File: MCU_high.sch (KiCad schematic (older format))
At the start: 0 parts

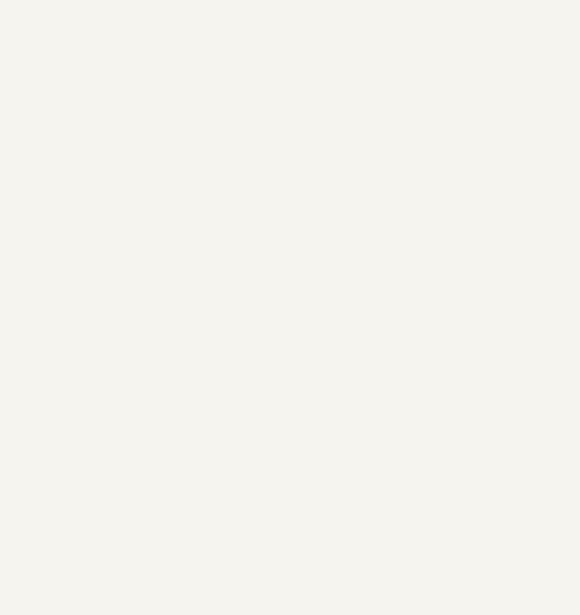
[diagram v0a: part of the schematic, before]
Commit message: - drivers modified - MCU replaced
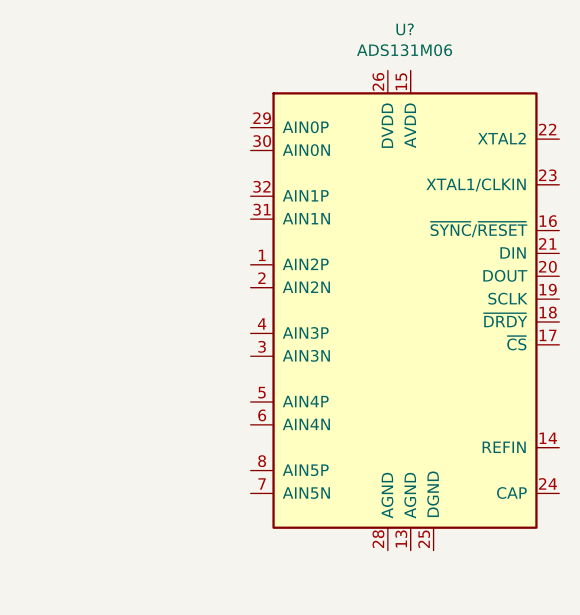
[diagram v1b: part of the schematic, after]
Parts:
- added U?: ADS131M06, miscellaneous_my:TQFP-32_5x5mm_P0.5mm_edges, symbol miscellaneous:ADS131M06
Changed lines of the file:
@@
 Text HLabel 2350 3500 0    50   Output ~ 0
 UART_TX
+$Comp
+L miscellaneous:ADS131M06 U?
+U 1 1 5F893814
+P 7850 2300
+F 0 "U?" H 7825 3528 50  0000 C CNN
+F 1 "ADS131M06" H 7825 3437 50  0000 C CNN
+F 2 "miscellaneous_my:TQFP-32_5x5mm_P0.5mm_edges" H 7850 2300 50  0001 C CNN
+F 3 "" H 7850 2300 50  0001 C CNN
+	1    7850 2300
+	1    0    0    -1
+$EndComp
 $EndSCHEMATC

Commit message: - high side (supply, MCU) - low side MCU - much small changes
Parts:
- removed U?: ADS131M06, miscellaneous_my:TQFP-32_5x5mm_P0.5mm_edges, symbol miscellaneous:ADS131M06
- added C? (x6): 100n, Capacitor_SMD:C_0603_1608Metric_Pad1.05x0.95mm_HandSolder, symbol Device:C_Small
- added C? (x6): 22p, Capacitor_SMD:C_0603_1608Metric_Pad1.05x0.95mm_HandSolder, symbol Device:C_Small
- added C?: 1u, Capacitor_SMD:C_0603_1608Metric_Pad1.05x0.95mm_HandSolder, symbol Device:C_Small
- added D?: RB520S30, miscellaneous_my:D_SOD-323-523_HandSoldering, symbol Device:D_Schottky_Small
- added J?: STLinkV2, miscellaneous_my:ST-LinkV2_FakeStm8Stm32_vertical, symbol Connector_Generic:Conn_02x05_Odd_Even
- added J?: Nucleo_SWD, Connector_PinSocket_2.54mm:PinSocket_1x06_P2.54mm_Vertical, symbol Connector:Conn_01x06_Female
- added L? (x2): BLM18TG102, Resistor_SMD:R_0603_1608Metric_Pad1.05x0.95mm_HandSolder, symbol Device:L_Core_Ferrite_Small
- added R?: 100k, Resistor_SMD:R_0603_1608Metric_Pad1.05x0.95mm_HandSolder, symbol Device:R_Small
- added R?: 0R, Resistor_SMD:R_0603_1608Metric_Pad1.05x0.95mm_HandSolder, symbol Device:R_Small
- added R?: 10R, Resistor_SMD:R_0603_1608Metric_Pad1.05x0.95mm_HandSolder, symbol Device:R_Small
- added SW?: RST, Button_Switch_SMD:SW_Push_1P1T_NO_6x6mm_H9.5mm, symbol Switch:SW_MEC_5E
- added U?: STM32L431RBTx, Package_QFP:LQFP-64_10x10mm_P0.5mm, symbol MCU_ST_STM32L4:STM32L431RBTx
- added U?: ADS131M06, miscellaneous_my:TQFP-32_5x5mm_P0.5mm_edges, symbol miscellaneous:ADS131M06
- added Y?: 8.192, Crystal:Crystal_HC49-4H_Vertical, symbol Device:Crystal_Small
- added Y?: 32.768, Crystal:Crystal_AT310_D3.0mm_L10.0mm_Horizontal_1EP_style2, symbol Device:Crystal_Small
- added Y?: 8.192, Crystal:Crystal_AT310_D3.0mm_L10.0mm_Horizontal_1EP_style2, symbol Device:Crystal_Small
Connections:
- new net: C?.2, U?.3 (PC14), Y?.1
- new net: C?.2, U?.4 (PC15), Y?.2
- new net: C?.1, U?.5 (PH0), Y?.1
- new net: C?.1, U?.6 (PH1), Y?.2
- new net: C?.1, U?.14 (REFIN)
- new net: C?.1, C?.1, L?.2, U?.15 (AVDD)
- new net: C?.1, U?.22 (XTAL2), Y?.2
- new net: C?.1, R?.1, U?.23 (XTAL1/CLKIN), Y?.1
- new net: C?.1, U?.24 (CAP)
- new net: C?.1, L?.1, L?.2
- new net: D?.2 (A), J?.1 (Pin_1), J?.8 (Pin_8)
- new net: D?.1 (K), R?.2
- new net ADC_CS: U?.17 (~CS), U?.21 (PA5)
- new net ADC_DRDY: U?.18 (~DRDY), U?.24 (PC4)
- new net ADC_MISO: U?.20 (DOUT), U?.22 (PA6)
- new net ADC_MOSI: U?.21 (DIN), U?.23 (PA7)
- new net ADC_RESET: U?.16 (~SYNC~/~RESET), U?.20 (PA4)
- new net ADC_SCK: U?.15 (PA1), U?.19 (SCLK)
- new net GND: J?.3 (Pin_3)
- new net HV+3V3: C?.1, L?.1, R?.1, R?.1, U?.26 (DVDD)
- new net HVGND: C?.1, C?.1, C?.1, C?.2, C?.2, C?.2, C?.2, C?.2, C?.2, C?.2, C?.2, C?.2, C?.2, J?.5 (Pin_5), J?.6 (Pin_6), SW?.1, SW?.2, U?.12 (VSSA), U?.13 (AGND), U?.18 (VSS), U?.25 (DGND), U?.28 (AGND), U?.31 (VSS), U?.47 (VSS), U?.63 (VSS)
- new net MCO: R?.2, U?.41 (PA8)
- new net NRST: C?.2, J?.5 (Pin_5), J?.9 (Pin_9), R?.2, SW?.3 (K), SW?.4 (A), U?.7 (NRST)
- new net SWD_CLK: J?.2 (Pin_2), J?.2 (Pin_2), U?.49 (PA14)
- new net SWD_IO: J?.4 (Pin_4), J?.4 (Pin_4), U?.46 (PA13)
- new net SWD_SWO: J?.6 (Pin_6), J?.7 (Pin_7), U?.55 (PB3)
- no-connect marks 0 -> 3

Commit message: - final schematic
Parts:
- added C159, C165, C166, C167, C168, C170: 1n, Capacitor_SMD:C_0603_1608Metric_Pad1.05x0.95mm_HandSolder, symbol Device:C_Small
- added C160, C161, C162, C163, C164: 100n, Capacitor_SMD:C_0603_1608Metric_Pad1.05x0.95mm_HandSolder, symbol Device:C_Small
- added D31: Green, Diode_SMD:D_0805_2012Metric_Pad1.15x1.40mm_HandSolder, symbol Device:LED_Small
- added D32: Orange, Diode_SMD:D_0805_2012Metric_Pad1.15x1.40mm_HandSolder, symbol Device:LED_Small
- added D33: Red, Diode_SMD:D_0805_2012Metric_Pad1.15x1.40mm_HandSolder, symbol Device:LED_Small
- added D34: Blue, Diode_SMD:D_0805_2012Metric_Pad1.15x1.40mm_HandSolder, symbol Device:LED_Small
- added R174, R176, R177, R178, R179, R181, R182: 0R, Resistor_SMD:R_0603_1608Metric_Pad1.05x0.95mm_HandSolder, symbol Device:R_Small
- added R183, R184, R185, R186: 1k, Resistor_SMD:R_0603_1608Metric_Pad1.05x0.95mm_HandSolder, symbol Device:R_Small
- added TP20, TP21, TP22, TP23: TestPoint, TestPoint:TestPoint_THTPad_D1.5mm_Drill0.7mm, symbol Connector:TestPoint
- gave numbers to parts that had none: 27
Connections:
- net HV+3V3: now also U34.13 (VDDA), U34.19 (VDD), U34.32 (VDD), U34.48 (VDDUSB), U34.64 (VDD), C160.2, C161.2, C162.2, C163.2, C164.2, R179.2
- net HVGND: now also U33.2 (AIN2N), U33.3 (AIN3N), U33.30 (AIN0N), U33.31 (AIN1N), U33.6 (AIN4N), U33.7 (AIN5N), C159.1, C160.1, C161.1, C162.1, C163.1, C164.1, C165.1, C166.1, C167.1, C168.1, C170.1, R183.2, R184.2, R185.2, R186.2
- net UART_RX: now also U34.59 (PB7)
- net UART_TX: now also U34.58 (PB6)
- net at U34.1 (VBAT): now also R179.1
- net LED_BLU: now reaches U34.50 (PA15)
- net LED_BLU: now also D34.2 (A)
- net LED_GRN: now reaches U34.51 (PC10)
- net LED_GRN: now also D31.2 (A)
- net LED_ORG: now reaches U34.52 (PC11)
- net LED_ORG: now also D32.2 (A)
- net LED_RED: now reaches U34.53 (PC12)
- net LED_RED: now also D33.2 (A)
- net at U33.1 (AIN2P): now also C166.2, R177.2
- net at U33.29 (AIN0P): now also C159.2, R174.2
- net at U33.32 (AIN1P): now also C165.2, R176.2
- net at U33.4 (AIN3P): now also C167.2, R178.2
- net at U33.5 (AIN4P): now also C168.2, R181.2
- net at U33.8 (AIN5P): now also C170.2, R182.2
- new net: D31.1 (K), R183.1
- new net: D32.1 (K), R184.1
- new net: D33.1 (K), R185.1
- new net: D34.1 (K), R186.1
- new net: R182.1, TP23.1
- new net: R181.1, TP22.1
- new net: R178.1, TP21.1
- new net: R177.1, TP20.1
- new net ADC_CH0: R174.1
- new net ADC_CH1: R176.1
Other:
- moved on the sheet: D30, J11, J12, R173

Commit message: - init PCB - fix last things in schematic
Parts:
- removed SW11: RST, Button_Switch_SMD:SW_Push_1P1T_NO_6x6mm_H9.5mm, symbol Switch:SW_MEC_5E
- added SW11: RST, Button_Switch_SMD:SW_Push_1P1T_NO_6x6mm_H9.5mm, symbol Switch:SW_Push
- added TP33, TP34, TP35, TP36, TP37, TP38, TP39, TP40, TP41, TP42, TP43, TP44, TP45, TP46: TestPoint, TestPoint:TestPoint_THTPad_D1.5mm_Drill0.7mm, symbol Connector:TestPoint
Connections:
- net HVGND: now also SW11.1
- net NRST: now also SW11.2
- net at U34.16 (PA2): now also TP33.1
- net at U34.17 (PA3): now also TP34.1
- net at U34.29 (PB10): now also TP41.1
- net at U34.30 (PB11): now also TP42.1
- net at U34.33 (PB12): now also TP43.1
- net at U34.34 (PB13): now also TP44.1
- net at U34.35 (PB14): now also TP45.1
- net at U34.36 (PB15): now also TP46.1
- net at U34.42 (PA9): now also TP35.1
- net at U34.43 (PA10): now also TP36.1
- net at U34.44 (PA11): now also TP37.1
- net at U34.45 (PA12): now also TP38.1
- net at U34.61 (PB8): now also TP39.1
- net at U34.62 (PB9): now also TP40.1

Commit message: - pcb placement, add 3dShapes
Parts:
- Y4: footprint Crystal:Crystal_AT310_D3.0mm_L10.0mm_Horizontal_1EP_style2 -> Crystal:Crystal_HC49-4H_Vertical
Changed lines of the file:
@@
 F 0 "Y4" H 10500 2400 50  0000 C CNN
 F 1 "8.192" H 10500 2300 50  0000 C CNN
-F 2 "Crystal:Crystal_AT310_D3.0mm_L10.0mm_Horizontal_1EP_style2" H 10500 2200 50  0001 C CNN
+F 2 "Crystal:Crystal_HC49-4H_Vertical" H 10500 2200 50  0001 C CNN
 F 3 "~" H 10500 2200 50  0001 C CNN
 	1    10500 2200

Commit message: - PCB progress
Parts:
- removed R179: 0R, Resistor_SMD:R_0603_1608Metric_Pad1.05x0.95mm_HandSolder, symbol Device:R_Small
- C153, C154, C155, C156, C157, C158, C159, C160, C161, C162, C163, C164, C165, C166, C167, C168, C169, C170, C171, C172, C173, C174, C175, C176: footprint Capacitor_SMD:C_0603_1608Metric_Pad1.05x0.95mm_HandSolder -> Capacitor_SMD:C_0603_1608Metric
- L14, L15: footprint Resistor_SMD:R_0603_1608Metric_Pad1.05x0.95mm_HandSolder -> Inductor_SMD:L_0603_1608Metric
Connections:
- net GND is gone; now on net HVGND: J12.3 (Pin_3)
- net HV+3V3: now also U34.1 (VBAT)

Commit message: - PCB WiP - Pump output aligned
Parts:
- R173, R174, R175, R176, R177, R178, R180, R181, R182, R183, R184, R185, R186: footprint Resistor_SMD:R_0603_1608Metric_Pad1.05x0.95mm_HandSolder -> Resistor_SMD:R_0603_1608Metric
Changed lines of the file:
@@
 F 0 "R180" H 3409 3396 50  0000 L CNN
 F 1 "100k" H 3409 3305 50  0000 L CNN
-F 2 "Resistor_SMD:R_0603_1608Metric_Pad1.05x0.95mm_HandSolder" H 3350 3350 50  0001 C CNN
+F 2 "Resistor_SMD:R_0603_1608Metric" H 3350 3350 50  0001 C CNN
 F 3 "~" H 3350 3350 50  0001 C CNN
 	1    3350 3350
@@
 F 0 "R175" V 10900 2500 50  0000 C BNN
 F 1 "0R" V 10700 2500 50  0000 C TNN
-F 2 "Resistor_SMD:R_0603_1608Metric_Pad1.05x0.95mm_HandSolder" V 10730 2500 50  0001 C CNN
+F 2 "Resistor_SMD:R_0603_1608Metric" V 10730 2500 50  0001 C CNN
 F 3 "~" H 10800 2500 50  0001 C CNN
 	1    10800 2500
@@
 F 0 "R173" H 2109 1146 50  0000 L CNN
 F 1 "10R" H 2109 1055 50  0000 L CNN
-F 2 "Resistor_SMD:R_0603_1608Metric_Pad1.05x0.95mm_HandSolder" H 2050 1100 50  0001 C CNN
+F 2 "Resistor_SMD:R_0603_1608Metric" H 2050 1100 50  0001 C CNN
 F 3 "~" H 2050 1100 50  0001 C CNN
 	1    2050 1100
@@
 F 0 "R183" H 959 3946 50  0000 L CNN
 F 1 "1k" H 959 3855 50  0000 L CNN
-F 2 "Resistor_SMD:R_0603_1608Metric_Pad1.05x0.95mm_HandSolder" H 900 3900 50  0001 C CNN
+F 2 "Resistor_SMD:R_0603_1608Metric" H 900 3900 50  0001 C CNN
 F 3 "~" H 900 3900 50  0001 C CNN
 	1    900  3900
@@
 F 0 "R184" H 1359 3946 50  0000 L CNN
 F 1 "1k" H 1359 3855 50  0000 L CNN
-F 2 "Resistor_SMD:R_0603_1608Metric_Pad1.05x0.95mm_HandSolder" H 1300 3900 50  0001 C CNN
+F 2 "Resistor_SMD:R_0603_1608Metric" H 1300 3900 50  0001 C CNN
 F 3 "~" H 1300 3900 50  0001 C CNN
 	1    1300 3900
@@
 F 0 "R185" H 1759 3946 50  0000 L CNN
 F 1 "1k" H 1759 3855 50  0000 L CNN
-F 2 "Resistor_SMD:R_0603_1608Metric_Pad1.05x0.95mm_HandSolder" H 1700 3900 50  0001 C CNN
+F 2 "Resistor_SMD:R_0603_1608Metric" H 1700 3900 50  0001 C CNN
 F 3 "~" H 1700 3900 50  0001 C CNN
 	1    1700 3900
@@
 F 0 "R186" H 2159 3946 50  0000 L CNN
 F 1 "1k" H 2159 3855 50  0000 L CNN
-F 2 "Resistor_SMD:R_0603_1608Metric_Pad1.05x0.95mm_HandSolder" H 2100 3900 50  0001 C CNN
+F 2 "Resistor_SMD:R_0603_1608Metric" H 2100 3900 50  0001 C CNN
 F 3 "~" H 2100 3900 50  0001 C CNN
 	1    2100 3900
@@
 F 0 "R174" V 8350 2250 50  0000 C BNN
 F 1 "0R" V 8150 2250 50  0000 C TNN
-F 2 "Resistor_SMD:R_0603_1608Metric_Pad1.05x0.95mm_HandSolder" V 8180 2250 50  0001 C CNN
+F 2 "Resistor_SMD:R_0603_1608Metric" V 8180 2250 50  0001 C CNN
 F 3 "~" H 8250 2250 50  0001 C CNN
 	1    8250 2250
@@
 F 0 "R176" V 8350 2550 50  0000 C BNN
 F 1 "0R" V 8150 2550 50  0000 C TNN
-F 2 "Resistor_SMD:R_0603_1608Metric_Pad1.05x0.95mm_HandSolder" V 8180 2550 50  0001 C CNN
+F 2 "Resistor_SMD:R_0603_1608Metric" V 8180 2550 50  0001 C CNN
 F 3 "~" H 8250 2550 50  0001 C CNN
 	1    8250 2550
@@
 F 0 "R182" V 8350 3750 50  0000 C BNN
 F 1 "0R" V 8150 3750 50  0000 C TNN
-F 2 "Resistor_SMD:R_0603_1608Metric_Pad1.05x0.95mm_HandSolder" V 8180 3750 50  0001 C CNN
+F 2 "Resistor_SMD:R_0603_1608Metric" V 8180 3750 50  0001 C CNN
 F 3 "~" H 8250 3750 50  0001 C CNN
 	1    8250 3750
@@
 F 0 "R181" V 8350 3450 50  0000 C BNN
 F 1 "0R" V 8150 3450 50  0000 C TNN
-F 2 "Resistor_SMD:R_0603_1608Metric_Pad1.05x0.95mm_HandSolder" V 8180 3450 50  0001 C CNN
+F 2 "Resistor_SMD:R_0603_1608Metric" V 8180 3450 50  0001 C CNN
 F 3 "~" H 8250 3450 50  0001 C CNN
 	1    8250 3450
@@
 F 0 "R178" V 8350 3150 50  0000 C BNN
 F 1 "0R" V 8150 3150 50  0000 C TNN
-F 2 "Resistor_SMD:R_0603_1608Metric_Pad1.05x0.95mm_HandSolder" V 8180 3150 50  0001 C CNN
+F 2 "Resistor_SMD:R_0603_1608Metric" V 8180 3150 50  0001 C CNN
 F 3 "~" H 8250 3150 50  0001 C CNN
 	1    8250 3150
@@
 F 0 "R177" V 8350 2850 50  0000 C BNN
 F 1 "0R" V 8150 2850 50  0000 C TNN
-F 2 "Resistor_SMD:R_0603_1608Metric_Pad1.05x0.95mm_HandSolder" V 8180 2850 50  0001 C CNN
+F 2 "Resistor_SMD:R_0603_1608Metric" V 8180 2850 50  0001 C CNN
 F 3 "~" H 8250 2850 50  0001 C CNN
 	1    8250 2850

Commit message: - PCB WiP
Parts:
- removed TP39, TP40: TestPoint, TestPoint:TestPoint_THTPad_D1.5mm_Drill0.7mm, symbol Connector:TestPoint
- added L22, L23, L24, L25, L26, L27: BLM18TG102, Inductor_SMD:L_0603_1608Metric, symbol Device:L_Core_Ferrite_Small
- Y6: footprint Crystal:Crystal_AT310_D3.0mm_L10.0mm_Horizontal_1EP_style2 -> Crystal:Crystal_C38-LF_D3.0mm_L8.0mm_Horizontal_1EP_style1; symbol Device:Crystal_Small -> Device:Crystal_GND3_Small
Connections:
- net ADC_CS: now also L27.1; no longer U33.17 (~CS)
- net ADC_DRDY: now also L26.2; no longer U33.18 (~DRDY)
- net ADC_MISO: now also L24.2; no longer U33.20 (DOUT)
- net ADC_MOSI: now also L23.2; no longer U33.21 (DIN)
- net ADC_RESET: now also L22.2; no longer U33.16 (~SYNC~/~RESET)
- net ADC_SCK: now also L25.2; no longer U33.19 (SCLK)
- net HVGND: now also C175.2, D31.1 (K), D32.1 (K), D33.1 (K), D34.1 (K), Y6.3; no longer C175.1, R183.2, R184.2, R185.2, R186.2
- net LED_BLU: now also R186.1; no longer D34.2 (A)
- net LED_GRN: now also R183.1; no longer D31.2 (A)
- net LED_ORG: now also R184.1; no longer D32.2 (A)
- net LED_RED: now also R185.1; no longer D33.2 (A)
- net at U34.3 (PC14), Y6.1: now also C175.1; no longer C175.2
- new net: L22.1, U33.16 (~SYNC~/~RESET)
- new net: L27.2, U33.17 (~CS)
- new net: L26.1, U33.18 (~DRDY)
- new net: L25.1, U33.19 (SCLK)
- new net: L24.1, U33.20 (DOUT)
- new net: L23.1, U33.21 (DIN)
- new net: D31.2 (A), R183.2
- new net: D32.2 (A), R184.2
- new net: D33.2 (A), R185.2
- new net: D34.2 (A), R186.2
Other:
- moved on the sheet: D31, D32, D33, D34, R183, R184, R185, R186
